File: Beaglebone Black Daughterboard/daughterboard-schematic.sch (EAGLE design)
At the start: 15 parts

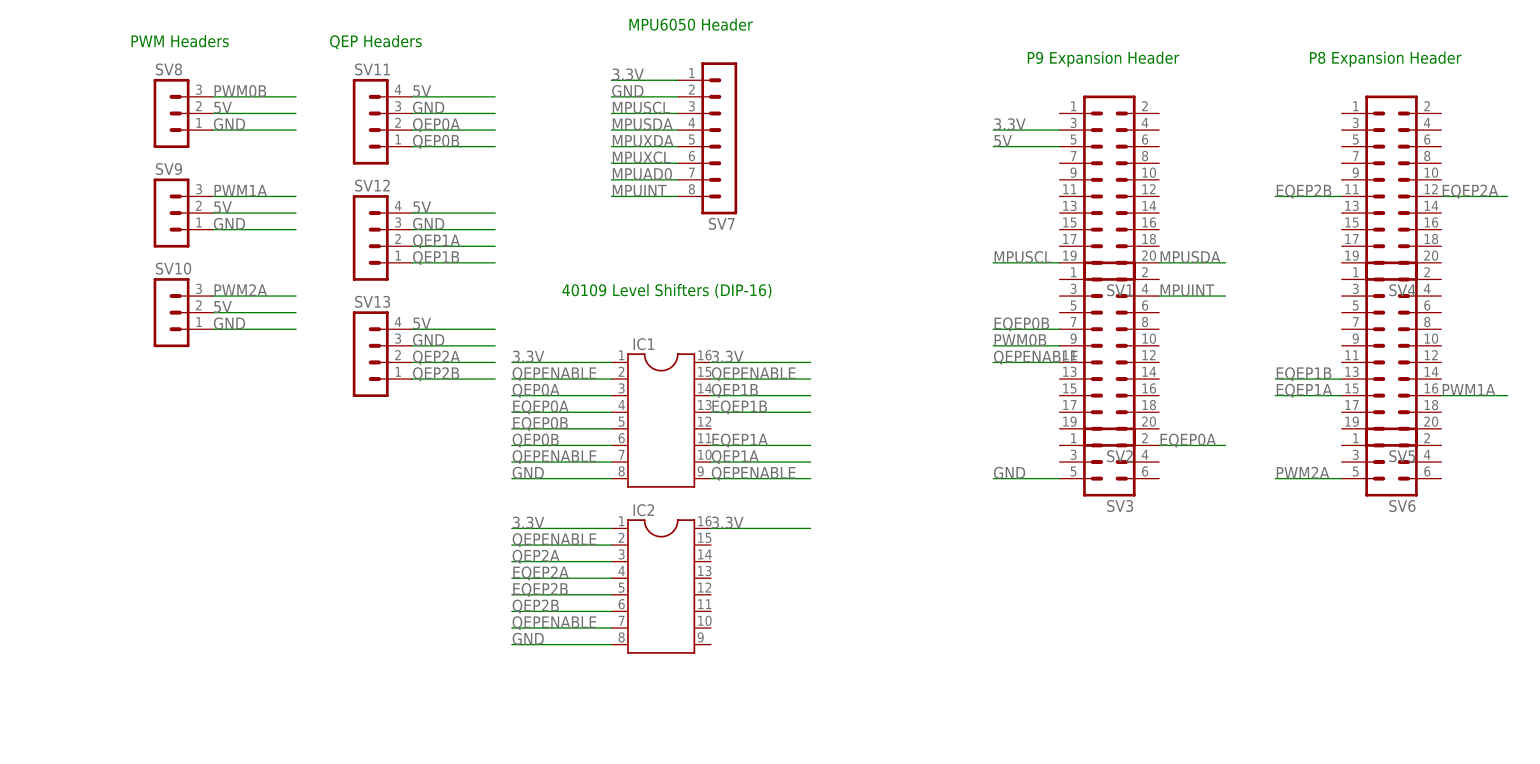
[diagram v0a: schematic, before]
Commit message: Replace P8 and P9 with single, custom pin headers. Minor cleanups.
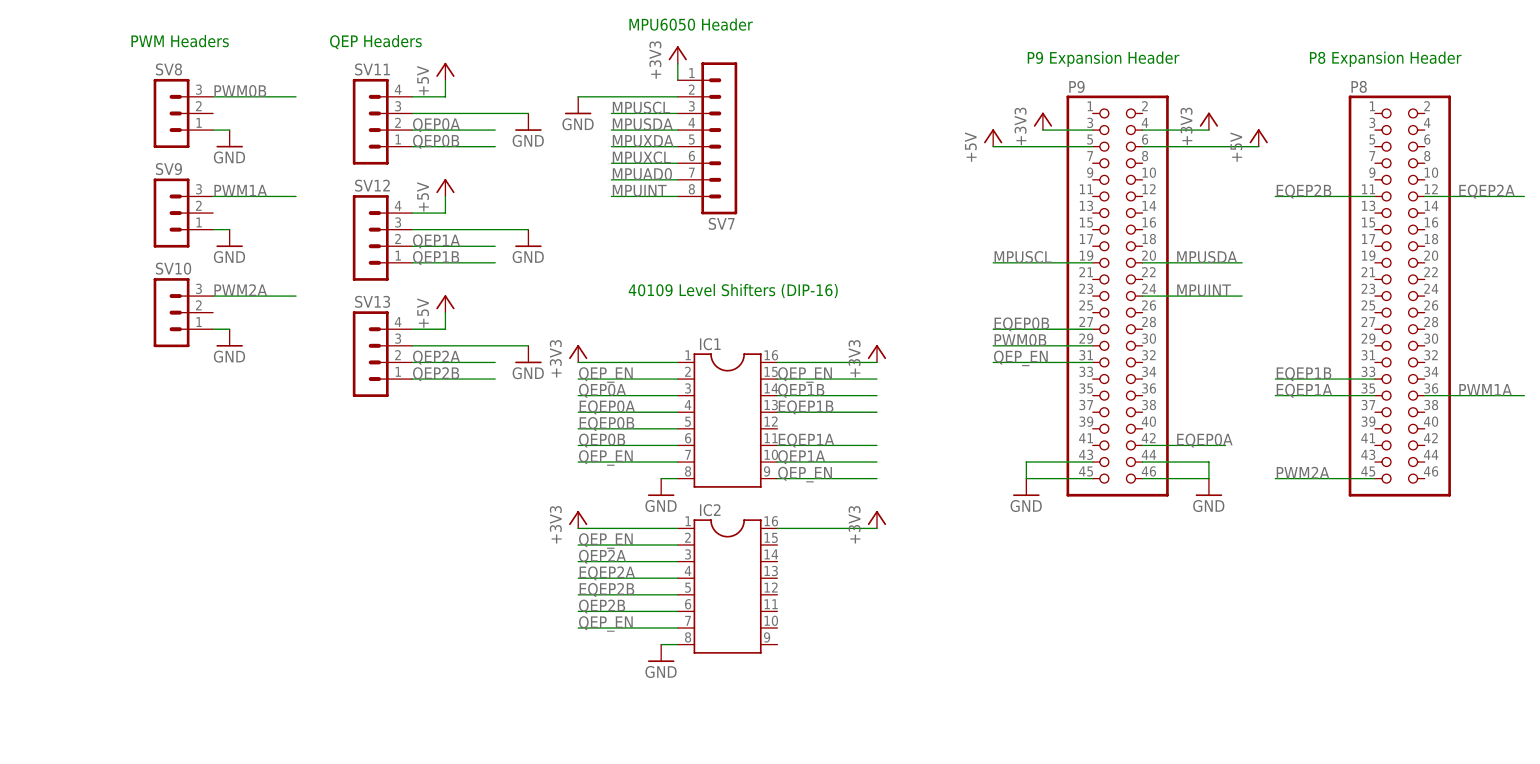
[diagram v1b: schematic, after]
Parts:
- removed SV1, SV2, SV4, SV5: (no value), con-lstb:MA10-2W
- removed SV3, SV6: (no value), con-lstb:MA03-2
- added P8, P9: (no value), pinheader-2x23:PINHD-2X23
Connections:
- removed net 3.3V: IC1.1, IC1.16, IC2.1, IC2.16, SV1.3, SV7.1
- removed net 5V: SV1.5, SV10.2, SV11.4, SV12.4, SV13.4, SV8.2, SV9.2
- removed net QEPENABLE: IC1.15, IC1.2, IC1.7, IC1.9, IC2.2, IC2.7, SV2.11
- new net +3V3: IC1.1, IC1.16, IC2.1, IC2.16, P9.3, P9.4, SV7.1
- new net +5V: P9.5, P9.6, SV11.4, SV12.4, SV13.4
- new net QEP_EN: IC1.15, IC1.2, IC1.7, IC1.9, IC2.2, IC2.7, P9.31
- net EQEP0A: now also P9.42; no longer SV3.2
- net EQEP0B: now also P9.27; no longer SV2.7
- net EQEP1A: now also P8.35; no longer SV5.15
- net EQEP1B: now also P8.33; no longer SV5.13
- net EQEP2A: now also P8.12; no longer SV4.12
- net EQEP2B: now also P8.11; no longer SV4.11
- net GND: now also P9.43, P9.44, P9.45, P9.46; no longer SV3.5
- net MPUINT: now also P9.24; no longer SV2.4
- net MPUSCL: now also P9.19; no longer SV1.19
- net MPUSDA: now also P9.20; no longer SV1.20
- net PWM0B: now also P9.29; no longer SV2.9
- net PWM1A: now also P8.36; no longer SV5.16
- net PWM2A: now also P8.45; no longer SV6.5
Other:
- moved on the sheet: IC1, IC2

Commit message: Insert EEPROM and encoder voltage jumpers.
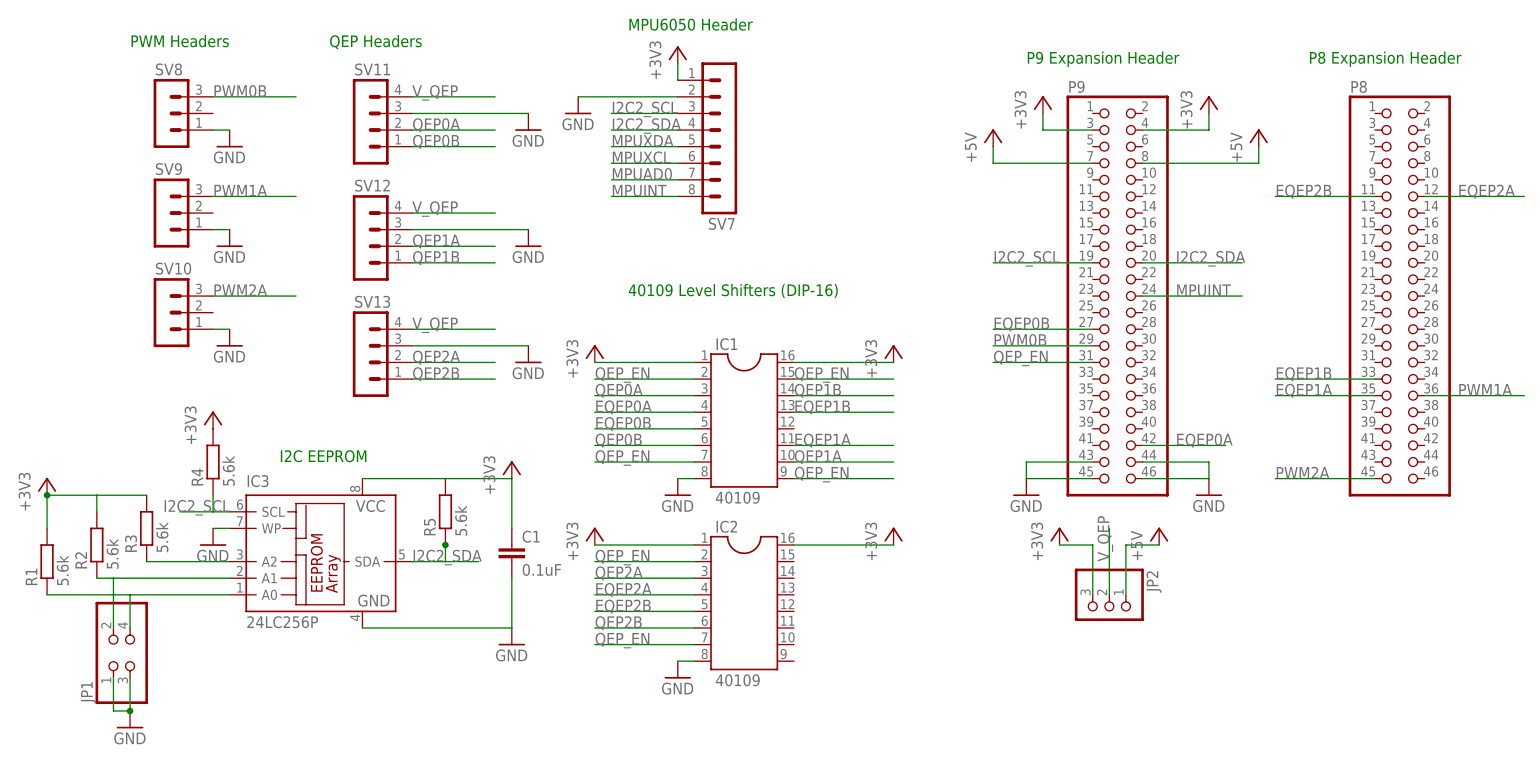
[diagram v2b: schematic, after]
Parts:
- added C1: 0.1uF, rcl:C-EU025-024X044
- added IC3: 24LC256P, microchip:24LC256P
- added JP1: (no value), pinhead:PINHD-2X2
- added JP2: (no value), pinhead:PINHD-1X3
- added R1, R2, R3, R4, R5: 5.6k, rcl:R-EU_0204/7
- IC1, IC2: value (none) -> 40109
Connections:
- removed net MPUSCL: P9.19, SV7.3
- removed net MPUSDA: P9.20, SV7.4
- new net I2C2_SCL: IC3.SCL, P9.19, R4.1, SV7.3
- new net I2C2_SDA: IC3.SDA, P9.20, R5.1, SV7.4
- new net N$3: IC3.A2, R3.1
- new net N$4: IC3.A1, JP1.2, R2.1
- new net N$5: IC3.A0, JP1.4, R1.1
- new net V_QEP: JP2.2, SV11.4, SV12.4, SV13.4
- net +3V3: now also C1.1, IC3.VCC, JP2.3, R1.2, R2.2, R3.2, R4.2, R5.2
- net +5V: now also JP2.1, P9.7, P9.8; no longer P9.5, P9.6, SV11.4, SV12.4, SV13.4
- net GND: now also C1.2, IC3.GND, IC3.WP, JP1.1, JP1.3
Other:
- note added: "I2C EEPROM"
- moved on the sheet: IC1, IC2
